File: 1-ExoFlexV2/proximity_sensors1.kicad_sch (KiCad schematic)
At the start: 37 parts, among them U37 SN74LVC3G14DCUT_V2, U38 SN74LVC3G14DCUT_V2, U39 SN74LVC3G14DCUT_V2, U40 SN74LVC3G14DCUT_V2, U43 SN74LVC1G08DBVR, U44 SN74LVC1G08DBVR, U45 SN74LVC1G08DBVR, U46 SN74LVC1G08DBVR, U47 SN74LVC3G14DCUT_V2

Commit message: Schématisation terminée
- Schéma terminé
- Passage vers le PCB
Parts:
- C37, C38, C39, C40: renamed from C?; value 10uF -> 10uF 10V X7R; DESCRIPTION (none) -> 10 µF ±10% 10V Ceramic Capacitor X7R 0805 (2012 Metric); MANUFACTURER (none) -> Murata Electronics; PACKAGE (none) -> 0805 (2012 Metric); PART NUMBER (none) -> GRM21BR71A106KA73L; TYPE (none) -> SMD
- C41, C42: renamed from C?; value * -> 10nF 10V X5R; footprint Capacitor_SMD:C_0805_2012Metric -> Capacitor_SMD:C_01005_0402Metric; DESCRIPTION (none) -> 10000 pF ±10% 10V Ceramic Capacitor X5R 01005 (0402 Metric); MANUFACTURER (none) -> Murata Electronics; NOTES (none) -> DO NOT POPULATE; PACKAGE (none) -> 01005 (0402 Metric); PART NUMBER (none) -> GRM022R61A103KE19L; TYPE (none) -> SMD
- J94, J95, J96, J97, J98, J99: renamed from J?; value Jmp -> Jumper; footprint (none) -> Connector_PinSocket_2.54mm:PinSocket_1x03_P2.54mm_Vertical; DESCRIPTION (none) -> CONN HEADER VERT 3POS 2.54MM; MANUFACTURER (none) -> Würth Elektronik; PACKAGE (none) -> Square 0.100" (2.54mm); PART NUMBER (none) -> 61300311121; TYPE (none) -> Through Hole
- R121, R122, R123, R124: renamed from R?; value 10k -> 10k 5% 1/8W; DESCRIPTION (none) -> 10 kOhms ±5% 0.125W, 1/8W Chip Resistor 0805 (2012 Metric) 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; MANUFACTURER (none) -> Panasonic Electronic Components; PACKAGE (none) -> 0805 (2012 Metric); PART NUMBER (none) -> ERJ-6GEYJ103V; TYPE (none) -> SMD
- R125, R126, R127, R128: renamed from R?; value 5k -> 5,1k 5% 1/8W; DESCRIPTION (none) -> 5.1 kOhms ±5% 0.125W, 1/8W Chip Resistor 0805 (2012 Metric)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; MANUFACTURER (none) -> Panasonic Electronic Components; PACKAGE (none) -> 0805 (2012 Metric); PART NUMBER (none) -> ERJ-6GEYJ512V; TYPE (none) -> SMD
- R129, R130: renamed from R?; DESCRIPTION (none) -> 0 Ohms Jumper Chip Resistor 0805 (2012 Metric) Automotive A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; MANUFACTURER (none) -> Panasonic Electronic Components; PACKAGE (none) -> 0805 (2012 Metric); PART NUMBER (none) -> ERJ-6GEY0R00V; TYPE (none) -> SMD
- R131, R132, R133, R134, R135, R136: renamed from R?; value 100k -> 100k 5% 1/8W; DESCRIPTION (none) -> 100 kOhms ±5% 0.125W, 1/8W Chip Resistor 0805 (2012 Metric)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; MANUFACTURER (none) -> Panasonic Electronic Components; PACKAGE (none) -> 0805 (2012 Metric); PART NUMBER (none) -> ERJ-6GEYJ104V; TYPE (none) -> SMD
- U58: renamed from U37; value SN74LVC3G14DCUT_V2 -> Inverter; DESCRIPTION (none) -> Inverter IC 3 Channel Schmitt Trigger 8-VSSOP; MANUFACTURER (none) -> Texas Instruments; PACKAGE (none) -> 8-VFSOP (0.091", 2.30mm Width); PART NUMBER (none) -> SN74LVC3G14DCUT; TYPE (none) -> SMD
- U59: renamed from U38; value SN74LVC3G14DCUT_V2 -> Inverter; DESCRIPTION (none) -> Inverter IC 3 Channel Schmitt Trigger 8-VSSOP; MANUFACTURER (none) -> Texas Instruments; PACKAGE (none) -> 8-VFSOP (0.091", 2.30mm Width); PART NUMBER (none) -> SN74LVC3G14DCUT; TYPE (none) -> SMD
- U60: renamed from U39; value SN74LVC3G14DCUT_V2 -> Inverter; DESCRIPTION (none) -> Inverter IC 3 Channel Schmitt Trigger 8-VSSOP; MANUFACTURER (none) -> Texas Instruments; PACKAGE (none) -> 8-VFSOP (0.091", 2.30mm Width); PART NUMBER (none) -> SN74LVC3G14DCUT; TYPE (none) -> SMD
- U61: renamed from U40; value SN74LVC3G14DCUT_V2 -> Inverter; DESCRIPTION (none) -> Inverter IC 3 Channel Schmitt Trigger 8-VSSOP; MANUFACTURER (none) -> Texas Instruments; PACKAGE (none) -> 8-VFSOP (0.091", 2.30mm Width); PART NUMBER (none) -> SN74LVC3G14DCUT; TYPE (none) -> SMD
- U62: renamed from U44; value SN74LVC1G08DBVR -> AND Gate; DESCRIPTION (none) -> AND Gate IC 1 Channel SOT-23-5; MANUFACTURER (none) -> Texas Instruments; PACKAGE (none) -> SC-74A, SOT-753; PART NUMBER (none) -> SN74LVC1G08DBVR; TYPE (none) -> SMD
- U63: renamed from U45; value SN74LVC1G08DBVR -> AND Gate; DESCRIPTION (none) -> AND Gate IC 1 Channel SOT-23-5; MANUFACTURER (none) -> Texas Instruments; PACKAGE (none) -> SC-74A, SOT-753; PART NUMBER (none) -> SN74LVC1G08DBVR; TYPE (none) -> SMD
- U64: renamed from U43; value SN74LVC1G08DBVR -> AND Gate; DESCRIPTION (none) -> AND Gate IC 1 Channel SOT-23-5; MANUFACTURER (none) -> Texas Instruments; PACKAGE (none) -> SC-74A, SOT-753; PART NUMBER (none) -> SN74LVC1G08DBVR; TYPE (none) -> SMD
- U65: renamed from U46; value SN74LVC1G08DBVR -> AND Gate; DESCRIPTION (none) -> AND Gate IC 1 Channel SOT-23-5; MANUFACTURER (none) -> Texas Instruments; PACKAGE (none) -> SC-74A, SOT-753; PART NUMBER (none) -> SN74LVC1G08DBVR; TYPE (none) -> SMD
- U66: renamed from U47; value SN74LVC3G14DCUT_V2 -> Inverter; DESCRIPTION (none) -> Inverter IC 3 Channel Schmitt Trigger 8-VSSOP; MANUFACTURER (none) -> Texas Instruments; PACKAGE (none) -> 8-VFSOP (0.091", 2.30mm Width); PART NUMBER (none) -> SN74LVC3G14DCUT; TYPE (none) -> SMD
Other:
- note added: "4xANDGate : 5V @ 128,04mA 5xNOTGate : 5V @ 160,05mA 6x100k : 5V @0,3mA 4x10k : 5V @ 2mA Total current : 5V @ 295mA"
- note removed: "4xANDGate : 5V @ 128,04mA 7xNOTGate : 5V @ 224,07mA 6x200k : 5V @0,15mA 4x10k : 5V @ 2mA Total current : 5V @ 360mA"
- moved on the sheet: J94, J95, J96, J97, R131, R132, R133, R134

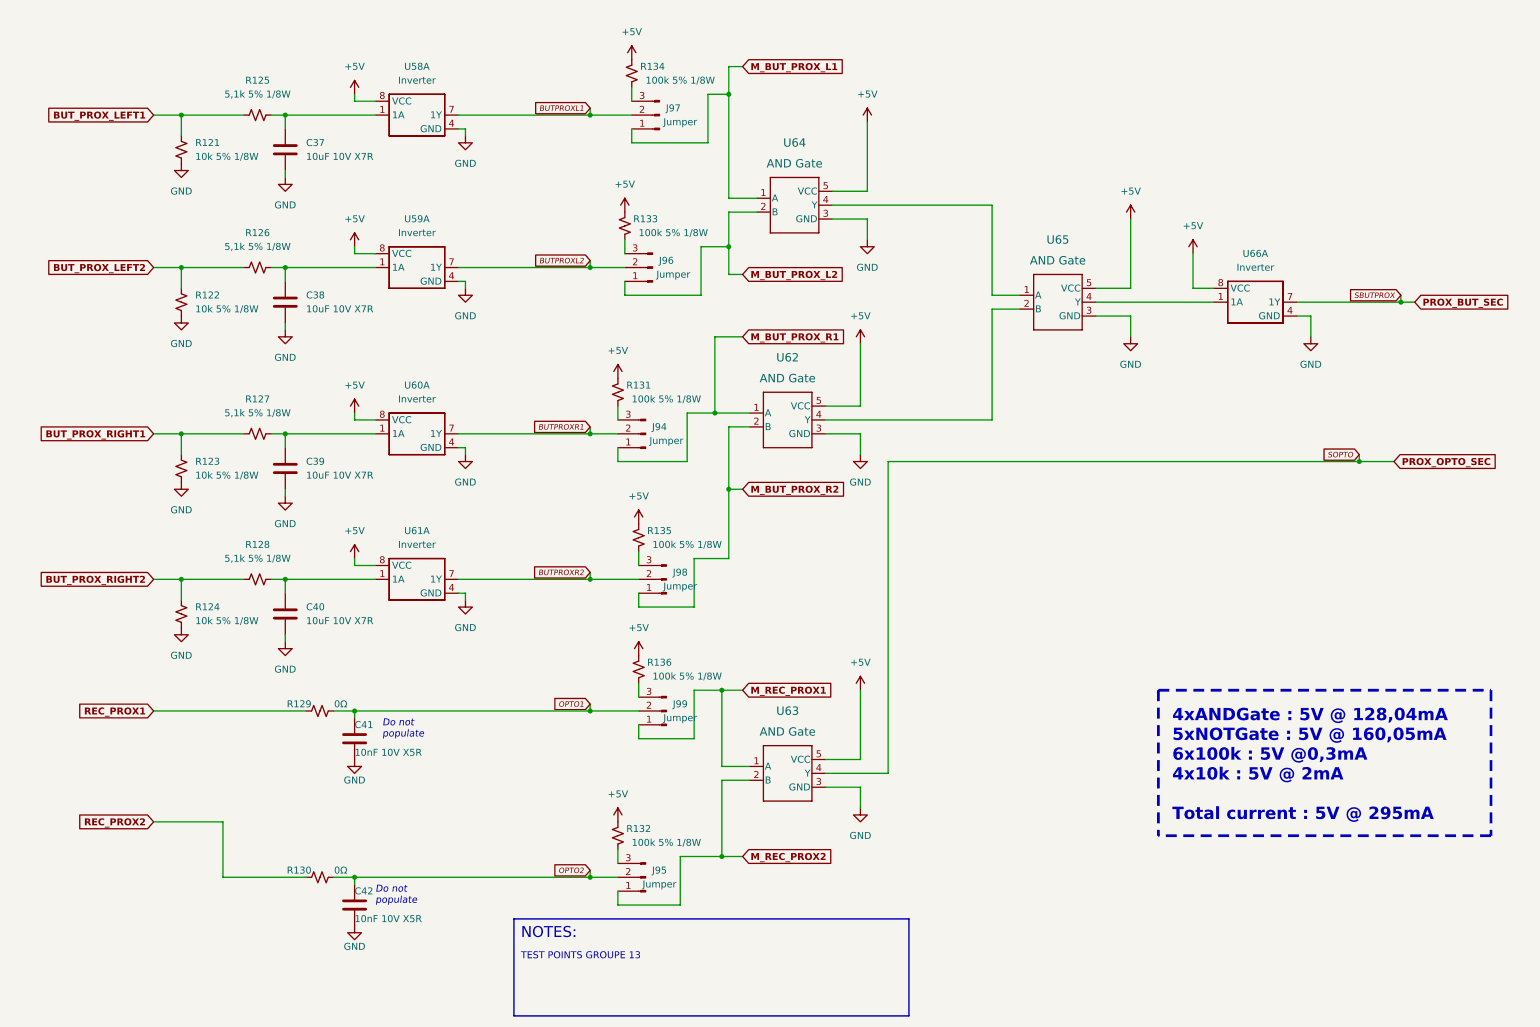
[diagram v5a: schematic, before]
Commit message: Finalisation 3
- Changement des régulateur de tension
- Retrait de test point inutile
- Changement de jumper mal positionner
- Ajout de Mounting holes et fiducial
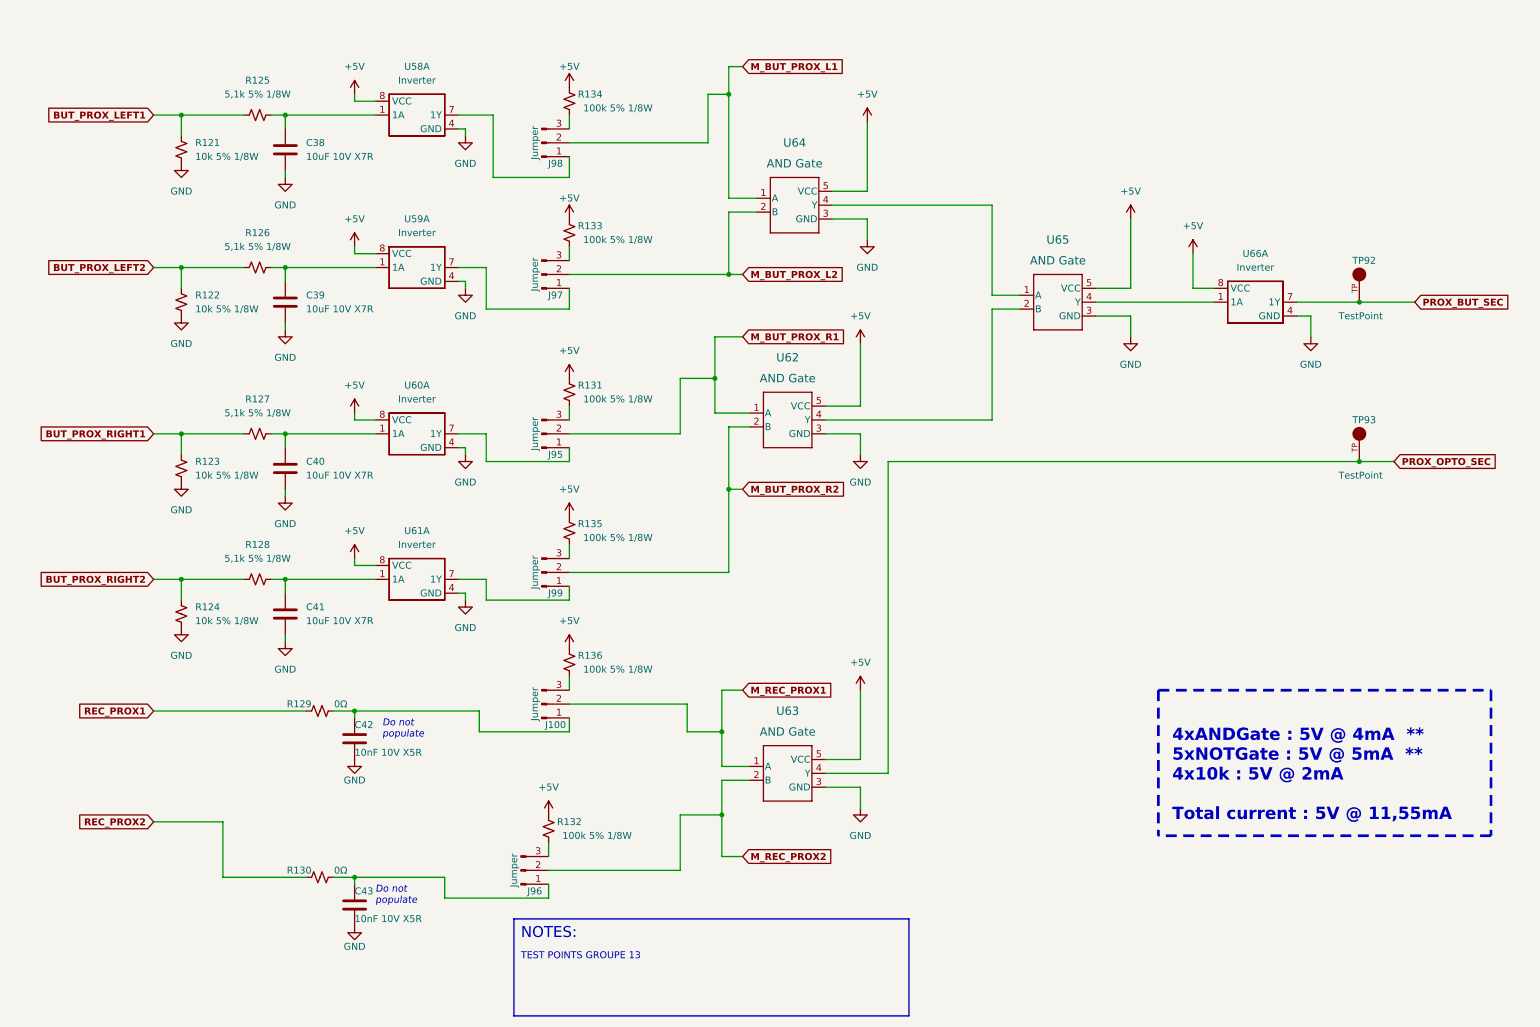
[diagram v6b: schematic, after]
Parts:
- removed C41: 10nF 10V X5R, Capacitor_SMD:C_01005_0402Metric, symbol Device:C
- added C43: 10nF 10V X5R, Capacitor_SMD:C_0603_1608Metric, symbol Device:C
- added TP92, TP93: TestPoint, FootPrint:KEYSTONE_5005, symbol SymLib:5005
- C42: footprint Capacitor_SMD:C_01005_0402Metric -> Capacitor_SMD:C_0603_1608Metric; DESCRIPTION 10000 pF ±10% 10V Ceramic Capacitor X5R 01005 (0402 Metric) -> 10000 pF ±5% 10V Ceramic Capacitor U2J 0603 (1608 Metric); PACKAGE 01005 (0402 Metric) -> 0603 (1608 Metric); PART NUMBER GRM022R61A103KE19L -> GRM1857U1A103JA44D
- J100: renamed from J99; footprint Connector_PinSocket_2.54mm:PinSocket_1x03_P2.54mm_Vertical -> Connector_PinHeader_2.54mm:PinHeader_1x03_P2.54mm_Vertical
- J95: renamed from J94; footprint Connector_PinSocket_2.54mm:PinSocket_1x03_P2.54mm_Vertical -> Connector_PinHeader_2.54mm:PinHeader_1x03_P2.54mm_Vertical
- J96: renamed from J95; footprint Connector_PinSocket_2.54mm:PinSocket_1x03_P2.54mm_Vertical -> Connector_PinHeader_2.54mm:PinHeader_1x03_P2.54mm_Vertical
- J97: renamed from J96; footprint Connector_PinSocket_2.54mm:PinSocket_1x03_P2.54mm_Vertical -> Connector_PinHeader_2.54mm:PinHeader_1x03_P2.54mm_Vertical
- J98: renamed from J97; footprint Connector_PinSocket_2.54mm:PinSocket_1x03_P2.54mm_Vertical -> Connector_PinHeader_2.54mm:PinHeader_1x03_P2.54mm_Vertical
- J99: renamed from J98; footprint Connector_PinSocket_2.54mm:PinSocket_1x03_P2.54mm_Vertical -> Connector_PinHeader_2.54mm:PinHeader_1x03_P2.54mm_Vertical
- renumbered C37 to C38, C38 to C39, C39 to C40, C40 to C41
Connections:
- net GND: now also C43.2
- net M_BUT_PROX_L1: now also J98.2 (Pin_2); no longer J98.1 (Pin_1)
- net M_BUT_PROX_L2: now also J97.2 (Pin_2); no longer J97.1 (Pin_1)
- net M_BUT_PROX_R1: now also J95.2 (Pin_2); no longer J95.1 (Pin_1)
- net M_BUT_PROX_R2: now also J99.2 (Pin_2); no longer J99.1 (Pin_1)
- net M_REC_PROX1: now also J100.2 (Pin_2); no longer J100.1 (Pin_1)
- net M_REC_PROX2: now also J96.2 (Pin_2); no longer J96.1 (Pin_1)
- net PROX_BUT_SEC: now also TP92.TP
- net PROX_OPTO_SEC: now also TP93.TP
- net BUTPROXL1: no longer names the net of U58.7 (1Y)
- net BUTPROXL1: now also J98.1 (Pin_1); no longer J98.2 (Pin_2)
- net BUTPROXL2: no longer names the net of U59.7 (1Y)
- net BUTPROXL2: now also J97.1 (Pin_1); no longer J97.2 (Pin_2)
- net BUTPROXR1: no longer names the net of U60.7 (1Y)
- net BUTPROXR1: now also J95.1 (Pin_1); no longer J95.2 (Pin_2)
- net BUTPROXR2: no longer names the net of U61.7 (1Y)
- net BUTPROXR2: now also J99.1 (Pin_1); no longer J99.2 (Pin_2)
- net OPTO1: no longer names the net of R129.2
- net OPTO1: now also C42.1, J100.1 (Pin_1); no longer J100.2 (Pin_2)
- removed net OPTO2: C42.1, J96.2 (Pin_2), R130.2
- new net: C43.1, J96.1 (Pin_1), R130.2
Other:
- note added: "4xANDGate : 5V @ 4mA ** 5xNOTGate : 5V @ 5mA ** 4x10k : 5V @ 2mA Total current : 5V @ 11,55mA"
- note removed: "4xANDGate : 5V @ 128,04mA 5xNOTGate : 5V @ 160,05mA 6x100k : 5V @0,3mA 4x10k : 5V @ 2mA Total current : 5V @ 295mA"
- moved on the sheet: J100, J95, J96, J97, J98, J99, R131, R132, R133, R134, R135, R136

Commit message: Finalisation schéma FIN
- Changement des uméro pour les inverseurs
- Changement des connecteur et début de placement
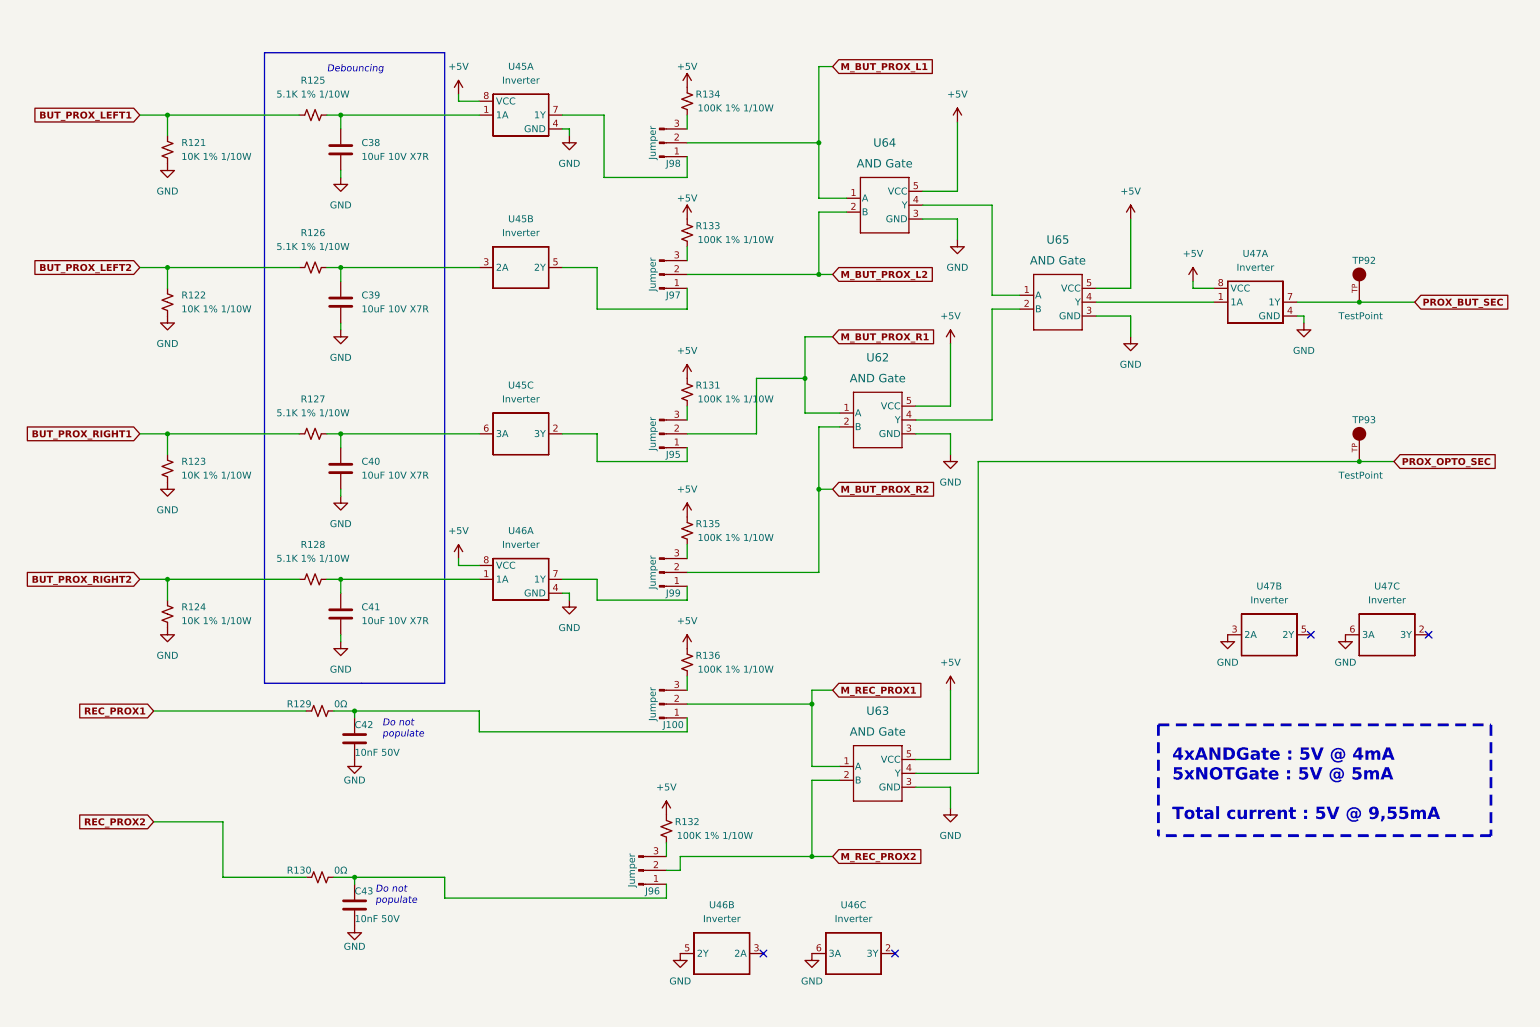
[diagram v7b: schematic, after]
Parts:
- removed U58, U59, U60, U61, U66: Inverter, FootPrint:SN74LVC3G14DCUT, symbol SymLib:SN74LVC3G14DCUT_V2
- added U45, U46, U47: Inverter, FootPrint:SN74LVC3G14DCUT, symbol SymLib:SN74LVC3G14DCUT_V2
- C42, C43: value 10nF 10V X5R -> 10nF 50V; footprint Capacitor_SMD:C_0603_1608Metric -> Capacitor_SMD:C_0805_2012Metric; DESCRIPTION 10000 pF ±5% 10V Ceramic Capacitor U2J 0603 (1608 Metric) -> 10000 pF ±5% 50V Ceramic Capacitor C0G, NP0 0805 (2012 Metr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; PACKAGE 0603 (1608 Metric) -> 0805 (2012 Metric); PART NUMBER GRM1857U1A103JA44D -> GRM2195C1H103JA01D
- R121, R122, R123, R124: value 10k 5% 1/8W -> 10K 1% 1/10W; footprint Resistor_SMD:R_0805_2012Metric -> Resistor_SMD:R_0603_1608Metric; DESCRIPTION 10 kOhms ±5% 0.125W, 1/8W Chip Resistor 0805 (2012 Metric) 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 -> 10 kOhms ±1% 0.1W, 1/10W Chip Resistor 0603 (1608 Metric) A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; PACKAGE 0805 (2012 Metric) -> 0603 (1608 Metric); PART NUMBER ERJ-6GEYJ103V -> ERJ-3EKF1002V
- R125, R126, R127, R128: value 5,1k 5% 1/8W -> 5.1K 1% 1/10W; footprint Resistor_SMD:R_0805_2012Metric -> Resistor_SMD:R_0603_1608Metric; DESCRIPTION 5.1 kOhms ±5% 0.125W, 1/8W Chip Resistor 0805 (2012 Metric)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 -> 5.1 kOhms ±1% 0.1W, 1/10W Chip Resistor 0603 (1608 Metric) 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; PACKAGE 0805 (2012 Metric) -> 0603 (1608 Metric); PART NUMBER ERJ-6GEYJ512V -> ERJ-3EKF5101V
- R131, R132, R133, R134, R135, R136: value 100k 5% 1/8W -> 100K 1% 1/10W; footprint Resistor_SMD:R_0805_2012Metric -> Resistor_SMD:R_0603_1608Metric; DESCRIPTION 100 kOhms ±5% 0.125W, 1/8W Chip Resistor 0805 (2012 Metric)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 -> 100 kOhms ±1% 0.1W, 1/10W Chip Resistor 0603 (1608 Metric) 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; PACKAGE 0805 (2012 Metric) -> 0603 (1608 Metric); PART NUMBER ERJ-6GEYJ104V -> ERJ-3EKF1003V
- TP92, TP93: NOTES (none) -> DO NOT POPULATE; PURCHASE-URL https://pricing.snapeda.com/search/part/5005/?ref=eda -> (none)
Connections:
- net +5V: now also U45.8 (VCC), U46.8 (VCC), U47.8 (VCC)
- net GND: now also U45.4 (GND), U46.4 (GND), U46.5 (2Y), U46.6 (3A), U47.3 (2A), U47.4 (GND), U47.6 (3A)
- net PROX_BUT_SEC: now also U47.7 (1Y)
- net at C41.1, R128.2: now also U46.1 (1A)
- net at J99.1 (Pin_1): now also U46.7 (1Y)
- net at C38.1, R125.2: now also U45.1 (1A)
- net at C40.1, R127.2: now also U45.6 (3A)
- net at J98.1 (Pin_1): now also U45.7 (1Y)
- net at U65.4 (Y): now also U47.1 (1A)
- net at C39.1, R126.2: now also U45.3 (2A)
- net at J97.1 (Pin_1): now also U45.5 (2Y)
- net at J95.1 (Pin_1): now also U45.2 (3Y)
- no-connect marks 0 -> 4
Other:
- note added: "4xANDGate : 5V @ 4mA 5xNOTGate : 5V @ 5mA Total current : 5V @ 9,55mA"
- note added: "Debouncing"
- note removed: "4xANDGate : 5V @ 4mA ** 5xNOTGate : 5V @ 5mA ** 4x10k : 5V @ 2mA Total current : 5V @ 11,55mA"
- note removed: "NOTES:"
- note removed: "TEST POINTS GROUPE 13"
- moved on the sheet: C38, C39, C40, C41, J100, J95, J96, J97, J98, J99, R121, R122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
